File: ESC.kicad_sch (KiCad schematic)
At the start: 1 part

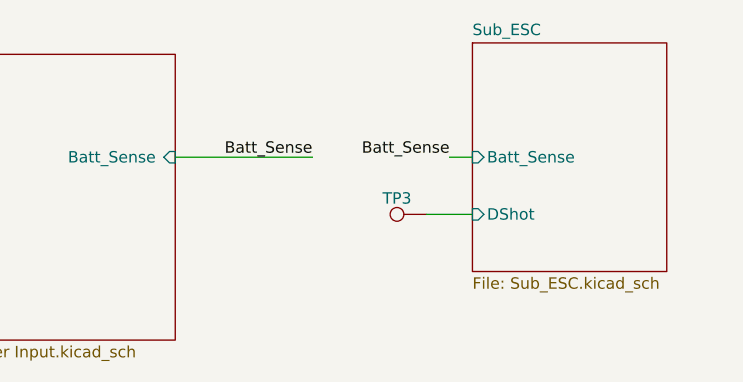
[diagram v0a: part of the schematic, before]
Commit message: Fixed pin names
reset pins to apply proper net names
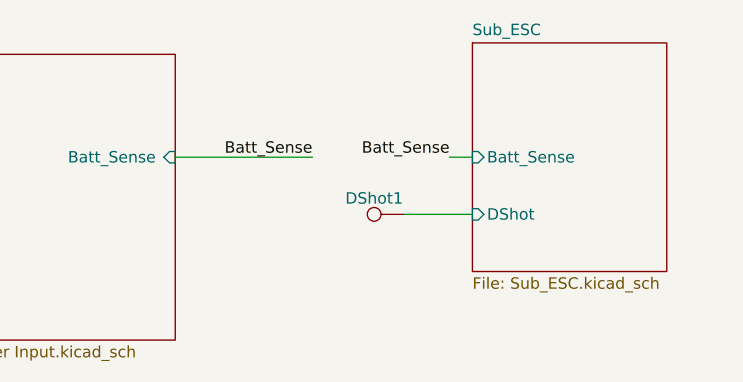
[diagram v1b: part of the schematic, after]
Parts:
- renumbered TP3 to DShot1
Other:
- moved on the sheet: DShot1
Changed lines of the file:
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@@
 	(wire
 		(pts
-			(xy 81.28 41.91) (xy 86.36 41.91)
+			(xy 78.74 41.91) (xy 86.36 41.91)
 		)
 		(stroke
@@
 		)
 	)
+	(netclass_flag ""
+		(length 2.54)
+		(shape round)
+		(at 80.01 41.91 180)
+		(fields_autoplaced yes)
+		(effects
+			(font
+				(size 1.27 1.27)
+			)
+			(justify right bottom)
+		)
+		(property "Netclass" "DShot"
+			(at 80.7085 44.45 0)
+			(effects
+				(font
+					(size 1.27 1.27)
+					(italic yes)
+				)
+				(justify left)
+			)
+		)
+	)
 	(symbol
 		(lib_id "Connector:TestPoint")
-		(at 81.28 41.91 90)
+		(at 78.74 41.91 90)
 		(unit 1)
 		(exclude_from_sim no)
@@
 		(on_board yes)
 		(dnp no)
-		(property "Reference" "TP3"
-			(at 77.978 40.132 90)
+		(property "Reference" "DShot1"
+			(at 75.438 40.132 90)
 			(effects
 				(font
@@
 		)
 		(property "Value" "TestPoint"
-			(at 77.978 39.37 90)
+			(at 75.438 39.37 90)
 			(effects
 				(font
@@
 		)
 		(property "Footprint" "TestPoint:TestPoint_Pad_1.0x1.0mm"
-			(at 81.28 36.83 0)
+			(at 78.74 36.83 0)
 			(effects
 				(font
@@
 		)
 		(property "Datasheet" "~"
-			(at 81.28 36.83 0)
+			(at 78.74 36.83 0)
 			(effects
 				(font
@@
 		)
 		(property "Description" "test point"
-			(at 81.28 41.91 0)
+			(at 78.74 41.91 0)
 			(effects
 				(font
@@
 			(project ""
 				(path "/0e826802-e676-4548-b85d-7973e5fc1500"
-					(reference "TP3")
+					(reference "DShot1")
 					(unit 1)
 				)

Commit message: more routing and placement
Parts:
- removed DShot1: TestPoint, TestPoint:TestPoint_Pad_1.0x1.0mm, symbol Connector:TestPoint
- added J1, J2: Conn_01x07, Connector_JST:JST_GH_BM07B-GHS-TBT_1x07-1MP_P1.25mm_Vertical, symbol Connector_Generic:Conn_01x07
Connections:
- new net +BATT: J1.7 (Pin_7)
- new net -BATT: J1.6 (Pin_6)
- new net DShot1: J1.1 (Pin_1)
- new net DShot2: J1.2 (Pin_2)
- new net DShot3: J1.3 (Pin_3)
- new net DShot4: J1.4 (Pin_4)
- new net SWD_CLK_1: J2.1 (Pin_1)
- new net SWD_CLK_2: J2.3 (Pin_3)
- new net SWD_CLK_3: J2.5 (Pin_5)
- new net SWD_CLK_4: J2.7 (Pin_7)
- new net SWD_IO_1: J2.2 (Pin_2)
- new net SWD_IO_2: J2.4 (Pin_4)
- new net SWD_IO_3: J2.6 (Pin_6)
- new net SWD_IO_4: J1.5 (Pin_5)
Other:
- added sheet Sub_ESC1 (Sub_ESC.kicad_sch)
- added sheet Sub_ESC2 (Sub_ESC.kicad_sch)
- added sheet Sub_ESC3 (Sub_ESC.kicad_sch)
- sheet Sub_ESC ports: added SWD_CLK_X, SWD_IO_X; removed none
